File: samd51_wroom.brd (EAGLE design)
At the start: 25.5 x 18 mm, 19 parts, among them X5 32.768

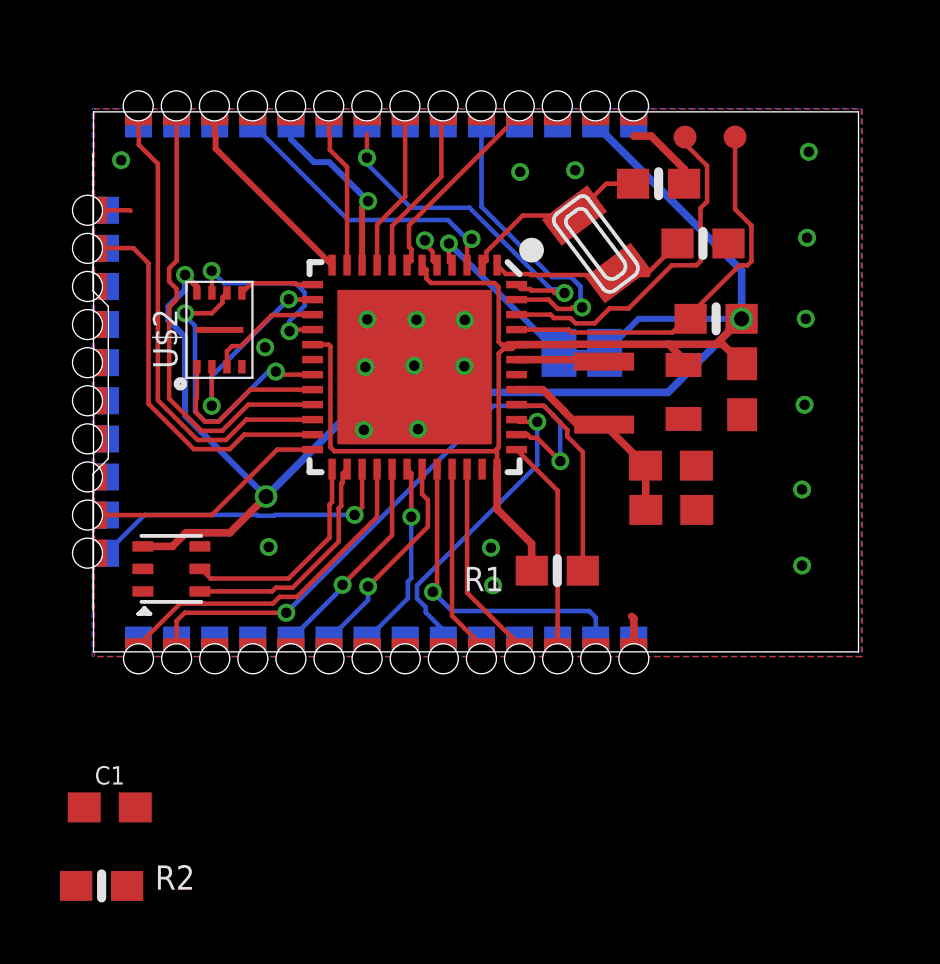
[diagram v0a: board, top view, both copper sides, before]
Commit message: added SWD and USB headers  :|
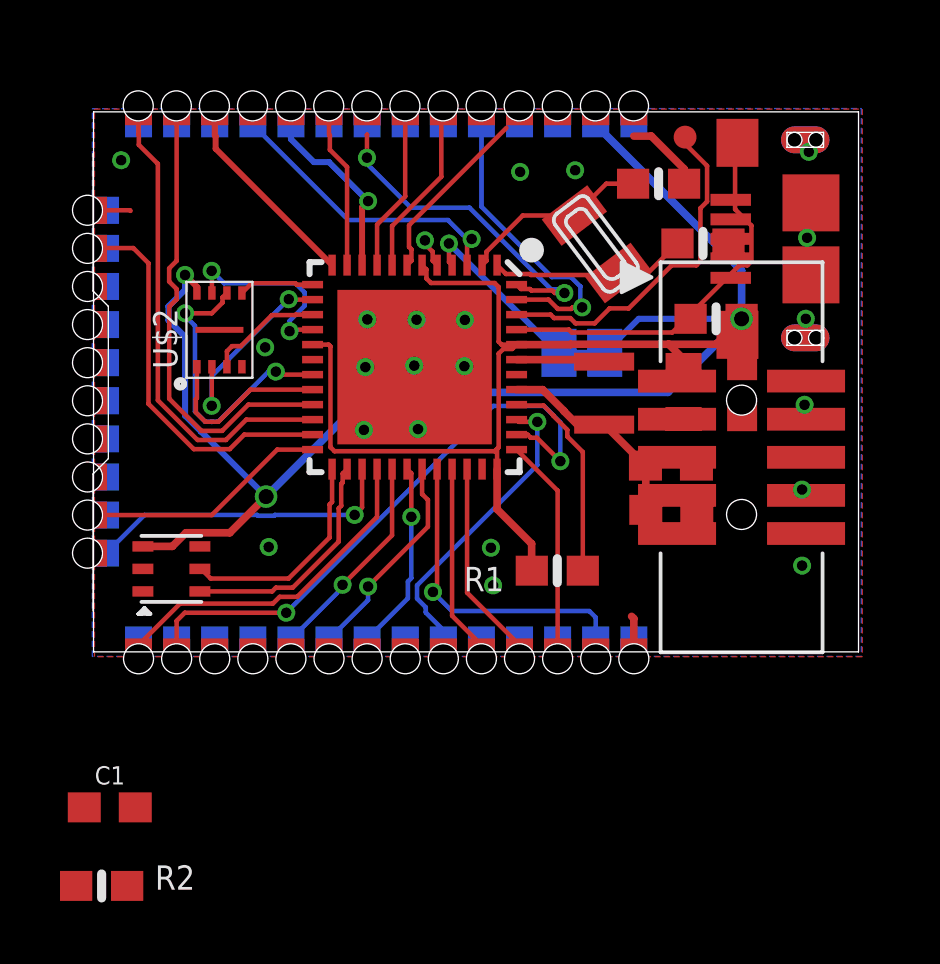
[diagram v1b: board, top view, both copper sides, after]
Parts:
- added U$15: AMPHENOL_MICRO_USB, 00_bsiepert:AMPHENOL_MICRO_USB
- added X2: 2x5 0.05" SWD, microbuilder:2X05_1.27MM_BOX_POSTS
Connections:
- net GND: now also X2.3, X2.5
- net RESET_SW: now also X2.10
- net SWCLK: now also X2.4
- net SWDIO: now also X2.2
- net VDDIO: now also X2.1
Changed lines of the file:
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@@
 </element>
 <element name="R2" library="microbuilder" package="0603-NO" value="330" x="0.281940625" y="-5.30098125"/>
+<element name="X2" library="microbuilder" package="2X05_1.27MM_BOX_POSTS" value="2x5 0.05&quot; SWD" x="21.612740625" y="8.98655" smashed="yes" rot="R270">
+<attribute name="VALUE" x="19.212740625" y="15.08655" size="0.4064" layer="27" ratio="10" rot="R270"/>
+</element>
+<element name="U$15" library="00_bsiepert" package="AMPHENOL_MICRO_USB" value="AMPHENOL_MICRO_USB" x="23.926803125" y="16.2687" rot="R90"/>
 </elements>
 <signals>
@@
 <via x="16.0655" y="18.554703125" extent="1-16" drill="0.35"/>
 <contactref element="C1" pad="1"/>
+<contactref element="X2" pad="3"/>
+<contactref element="X2" pad="5"/>
 <wire x1="23.7972625" y1="16.3042625" x2="23.85568125" y2="19.16938125" width="0" layer="19" extent="1-1"/>
 <wire x1="21.176275" y1="16.114828125" x2="23.7972625" y2="16.3042625" width="0" layer="19" extent="1-1"/>
@@
 <wire x1="21.632103125" y1="10.407025" x2="23.713440625" y2="10.736584375" width="0" layer="19" extent="1-1"/>
 <wire x1="19.679509375" y1="10.264115625" x2="21.632103125" y2="10.407025" width="0" layer="19" extent="1-1"/>
-<wire x1="20.109253125" y1="8.70931875" x2="19.679509375" y2="10.264115625" width="0" layer="19" extent="1-1"/>
+<wire x1="19.462740625" y1="10.25655" x2="19.679509375" y2="10.264115625" width="0" layer="19" extent="1-1"/>
+<wire x1="19.462740625" y1="8.98655" x2="19.462740625" y2="10.25655" width="0" layer="19" extent="1-1"/>
+<wire x1="20.109253125" y1="8.70931875" x2="19.462740625" y2="8.98655" width="0" layer="19" extent="1-1"/>
 <wire x1="20.12011875" y1="7.234584375" x2="20.109253125" y2="8.70931875" width="0" layer="19" extent="1-1"/>
 <wire x1="23.629621875" y1="7.912103125" x2="23.713440625" y2="10.736584375" width="0" layer="19" extent="1-1"/>
@@
 <wire x1="16.07958125" y1="13.4519125" x2="16.7165875" y2="13.4519125" width="0.1524" layer="1"/>
 <wire x1="16.7165875" y1="13.4519125" x2="17.214290625" y2="13.949615625" width="0.1524" layer="1"/>
+<contactref element="X2" pad="2"/>
+<wire x1="20.242375" y1="15.52014375" x2="23.762740625" y2="11.52655" width="0" layer="19" extent="1-1"/>
 </signal>
 <signal name="XOSC32_A">
@@
 <wire x1="21.6141625" y1="13.602665625" x2="18.184825" y2="13.602665625" width="0.2032" layer="16"/>
 <wire x1="18.184825" y1="13.602665625" x2="17.051015625" y2="12.46885625" width="0.2032" layer="16"/>
+<contactref element="X2" pad="1"/>
 <wire x1="16.75191875" y1="20.07611875" x2="16.75191875" y2="20.27611875" width="0" layer="19" extent="1-16"/>
+<wire x1="19.462740625" y1="11.52655" x2="19.162096875" y2="11.1506" width="0" layer="19" extent="1-16"/>
 </signal>
 <signal name="AREF">
@@
 <wire x1="21.54319375" y1="15.38623125" x2="19.304075" y2="13.1471125" width="0.1524" layer="1"/>
 <wire x1="19.304075" y1="13.1471125" x2="15.953325" y2="13.1471125" width="0.1524" layer="1"/>
+<contactref element="X2" pad="4"/>
+<wire x1="19.9141625" y1="13.602665625" x2="23.762740625" y2="10.25655" width="0" layer="19" extent="1-1"/>
 <wire x1="19.304075" y1="13.1471125" x2="19.9141625" y2="13.602665625" width="0" layer="19" extent="1-1"/>
 </signal>
@@
 <signal name="RESET_SW">
 <contactref element="R2" pad="2"/>
+<contactref element="X2" pad="10"/>
+<wire x1="1.131940625" y1="-5.30098125" x2="23.762740625" y2="6.44655" width="0" layer="19" extent="1-1"/>
 </signal>
 </signals>

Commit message: fully routed?
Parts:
- removed R9: 1K, microbuilder:0603-NO
- removed TP1, TP2: TEST-POINT3, SparkFun-Connectors:PAD.03X.03
- removed X2: 2x5 0.05" SWD, microbuilder:2X05_1.27MM_BOX_POSTS
- added R3: 1K, microbuilder:0603-NO
- added U$16: WINDBOND_QSPI_FLASHWSON_6X5, 00_bsiepert:WSON_6X5MM
- U$2: value WINDBOND_QSPI_FLASHUSON_2X3 -> SWD_HEADER; device 00_bsiepert:USON_2X3MM -> 00_bsiepert:AMPHENOL_SWD
- moved R2 19.9 mm to (16.9, 5.62)
- moved U$2 19.1 mm to (22.0, 6.10), turned to 180 degrees
- moved C1 17.8 mm to (17.0, 4.08), turned to 180 degrees
- moved SJ1 6.13 mm to (15.7, 18.6)
- moved C12 3.35 mm to (17.3, 17.5)
- moved X5 2.79 mm to (14.2, 17.2)
- moved C13 2.74 mm to (16.3, 19.1)
- moved C7 2.22 mm to (17.4, 9.85)
- moved C8 2.01 mm to (17.4, 7.87)
- moved R1 1.78 mm to (13.7, 5.33)
- moved C6 1.69 mm to (19.3, 12.8)
- moved L1 1.02 mm to (17.2, 12.1)
- moved C2 0.99 mm to (22.5, 10.8), turned to 0 degrees
- moved U$15 0.28 mm to (24.1, 16.0)
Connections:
- new net N$4: U$1.41
- net GND: now also U$15.P$5, U$16.4, U$2.P$3, U$2.P$5, U$2.P$9; no longer U$2.4, X2.3, X2.5
- net QSPI_CS: now also U$16.1; no longer U$2.1
- net QSPI_IO0: now also U$16.5; no longer U$2.5
- net QSPI_IO1: now also U$16.2; no longer U$2.2
- net QSPI_IO2: now also U$16.3; no longer U$2.3
- net QSPI_IO3: now also U$16.7; no longer U$2.7
- net QSPI_SCK: now also U$16.6; no longer U$2.6
- net RESET_SW: now also U$2.P$10; no longer X2.10
- net SWCLK: now also R3.1, U$2.P$4; no longer R9.1, TP1.P$1, X2.4
- net SWDIO: now also U$2.P$2; no longer TP2.P$1, X2.2
- net USB+: now also U$15.P$3
- net USB-: now also U$15.P$2
- net VDDCORE: no longer U$1.41
- net VDDIO: now also R3.2, U$16.8, U$2.P$1; no longer R9.2, U$2.8, X2.1
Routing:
- net USB+: track 6.59 -> 24.7 mm, vias 0 -> 2
- net USB-: track 6.27 -> 22.3 mm, vias 0 -> 2
- net SWCLK: track 13.2 -> 24.3 mm, vias 0 -> 2
- net SWDIO: track 11.6 -> 22.6 mm, vias 0 -> 3
- net GND: track 5.62 -> 11.4 mm, vias 22 -> 18
- net VDDIO: track 79.8 -> 75.0 mm, vias 3 -> 7
- net XOSC32_A: track 8.60 -> 3.84 mm
- net AREF: track 5.94 -> 10.1 mm
- net !RESET: track 6.96 -> 11.0 mm
- net QSPI_IO3: track 6.43 -> 10.2 mm
- net QSPI_IO0: track 2.51 -> 4.80 mm
- net QSPI_IO1: track 6.72 -> 4.61 mm, vias 2 -> 0
- net RESET_SW: track 0.00 -> 2.09 mm
- net IO39: track 9.86 -> 7.83 mm
- net IO21: track 9.69 -> 10.9 mm
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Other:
- board text removed: "/Users/bsiepert/Desktop/bitty.bmp"
